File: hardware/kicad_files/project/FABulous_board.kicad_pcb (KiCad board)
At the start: 4 copper layers, 101.2 x 63.5 mm, 85 parts, among them J1 Conn_01x03_Pin, J10 Conn_01x07_Pin, J11 Conn_01x03_Pin, J12 Conn_01x03_Pin, J13 Conn_01x03_Pin, J2 Conn_01x03_Pin, J3 Conn_01x03_Pin, J4 Conn_01x03_Pin, J5 Conn_01x02_Pin, J6 Conn_02x04_Odd_Even, J7 Conn_02x12_Odd_Even, J8 Conn_01x03_Pin, J9 Conn_01x05_Pin, SW1 Tactile Switch, T1 LOGO, T2 LOGO, T3 LOGO, T4 LOGO, T5 LOGO, U1 W25Q32JVSSIQ, U10 SN74LVC1G125DCKR, U11 SI5351A-B-GTR, U2 C2977809, U4 GT-USB-7010ASV, U5 FT232H, U6 AMS1117-3_3, U7 SPX1117M3-L_TR, U8 MCP1319MT-29LE-OT, U9 SN74LVC1G125DCKR, X1 TXM12M0004252DBCEO00T, X2 NX3225GA-25_000M-STD-CRG-2

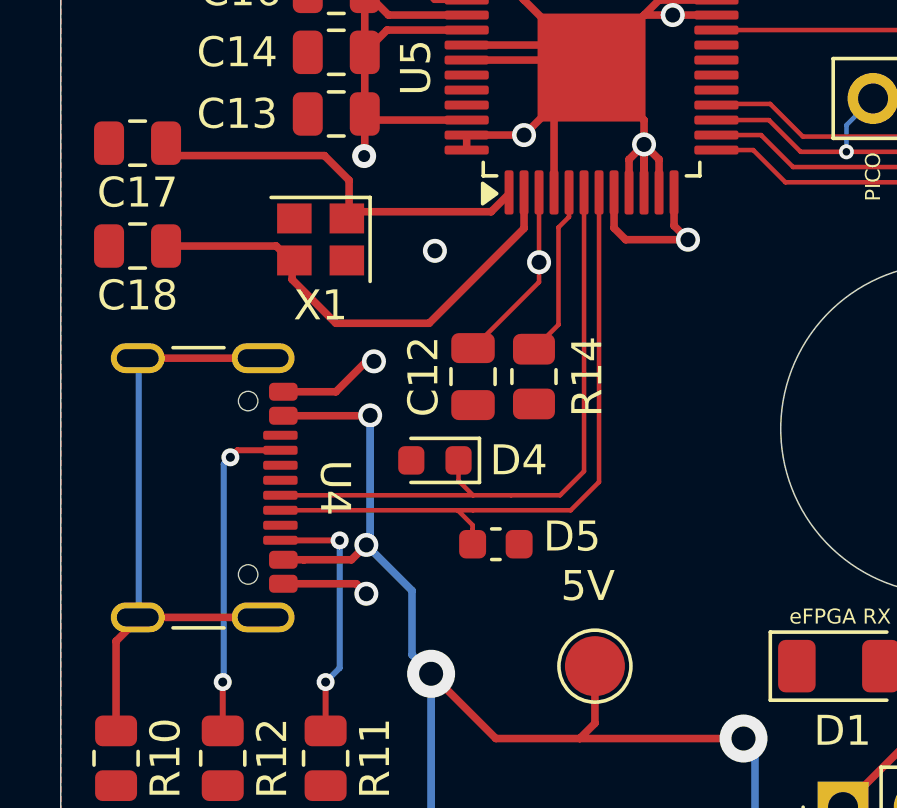
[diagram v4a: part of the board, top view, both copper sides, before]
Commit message: fix: add a connection to the addtional D+ and D- terminals to allow a reversible plugging of the connector, route the USB data line using an impedance matched differential pair
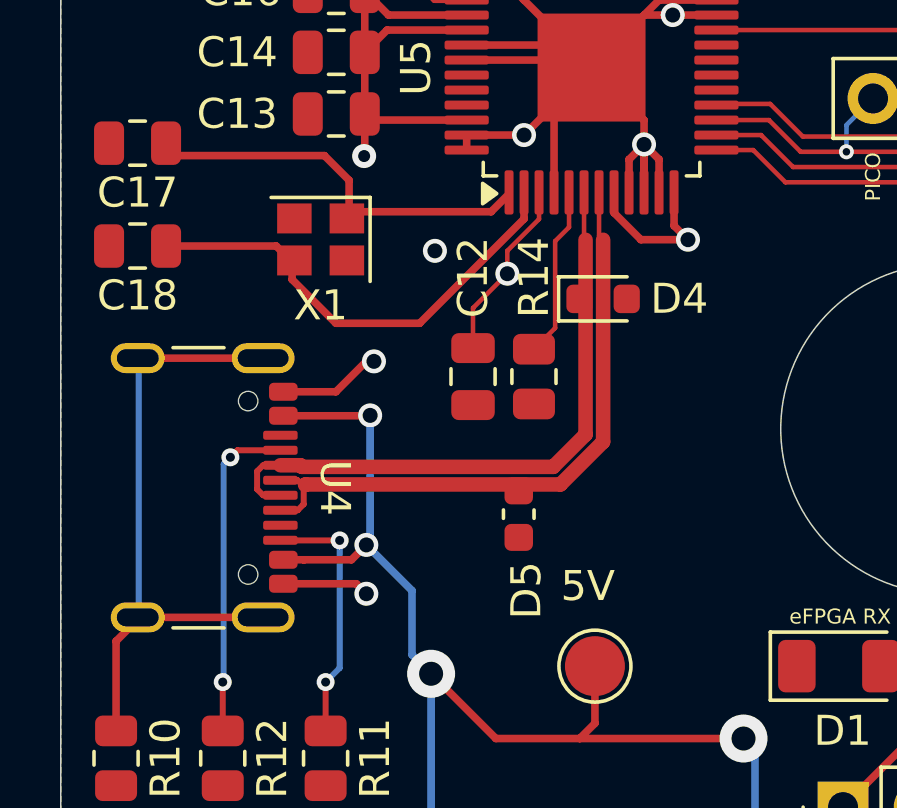
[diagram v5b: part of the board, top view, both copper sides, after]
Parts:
- moved D4 7.77 mm to (121.7, 91.6), turned to 0 degrees
- moved D5 1.26 mm to (118.9, 98.8), turned to -90 degrees
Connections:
- U4 pad A6: unconnected-(U4-D+-PadA6) -> /PC Connection/D+
- U4 pad B7: unconnected-(U4-D--PadB7) -> /PC Connection/D-
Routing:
- net /PC Connection/D+: track 22.0 -> 21.2 mm
